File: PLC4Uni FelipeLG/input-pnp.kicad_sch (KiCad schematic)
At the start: 3 parts, among them Q3 2SA2018

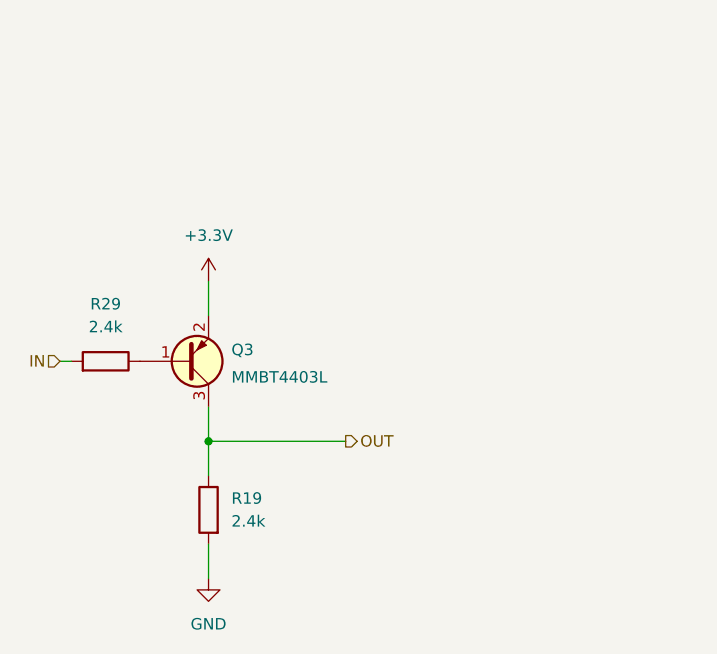
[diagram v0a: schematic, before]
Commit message: Add files via upload
Updated Circuitos corregidos y pistas agregadas
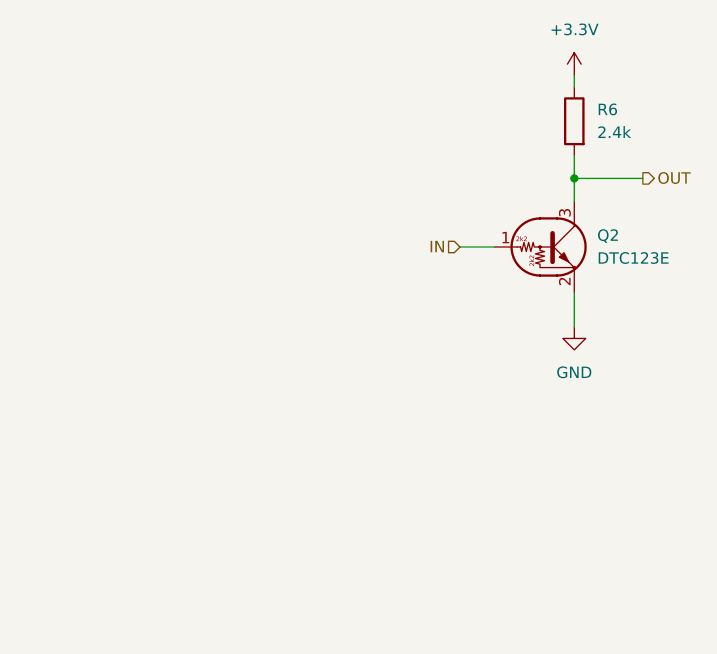
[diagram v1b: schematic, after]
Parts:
- removed Q3: 2SA2018, Package_TO_SOT_SMD_AKL:SOT-416, symbol Transistor_BJT_AKL:2SA2018
- removed R19, R29: 2.4k, Resistor_SMD_AKL:R_0603_1608Metric, symbol Resistor_AKL:R_0603
- added Q2: DTC123E, Package_TO_SOT_SMD:SOT-23, symbol Transistor_BJT:DTC123E
- added R6: 2.4k, Resistor_SMD_AKL:R_0603_1608Metric, symbol Resistor_AKL:R_0603
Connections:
- net +3.3V: now also R6.2
- net GND: now also Q2.2 (E)
- net IN: now also Q2.1 (B)
- net OUT: now also Q2.3 (C), R6.1
